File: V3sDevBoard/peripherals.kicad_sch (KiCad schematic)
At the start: 52 parts, among them J9 GPIO, SW1 BUT6, SW2 BUT1, SW3 BUT2, SW4 BUT3, SW5 BUT4, SW6 BUT5, U10 MPU-6050, U11 BME280, U8 ESP32-WROOM-32, U9 Ai-Thinker-Ra-02

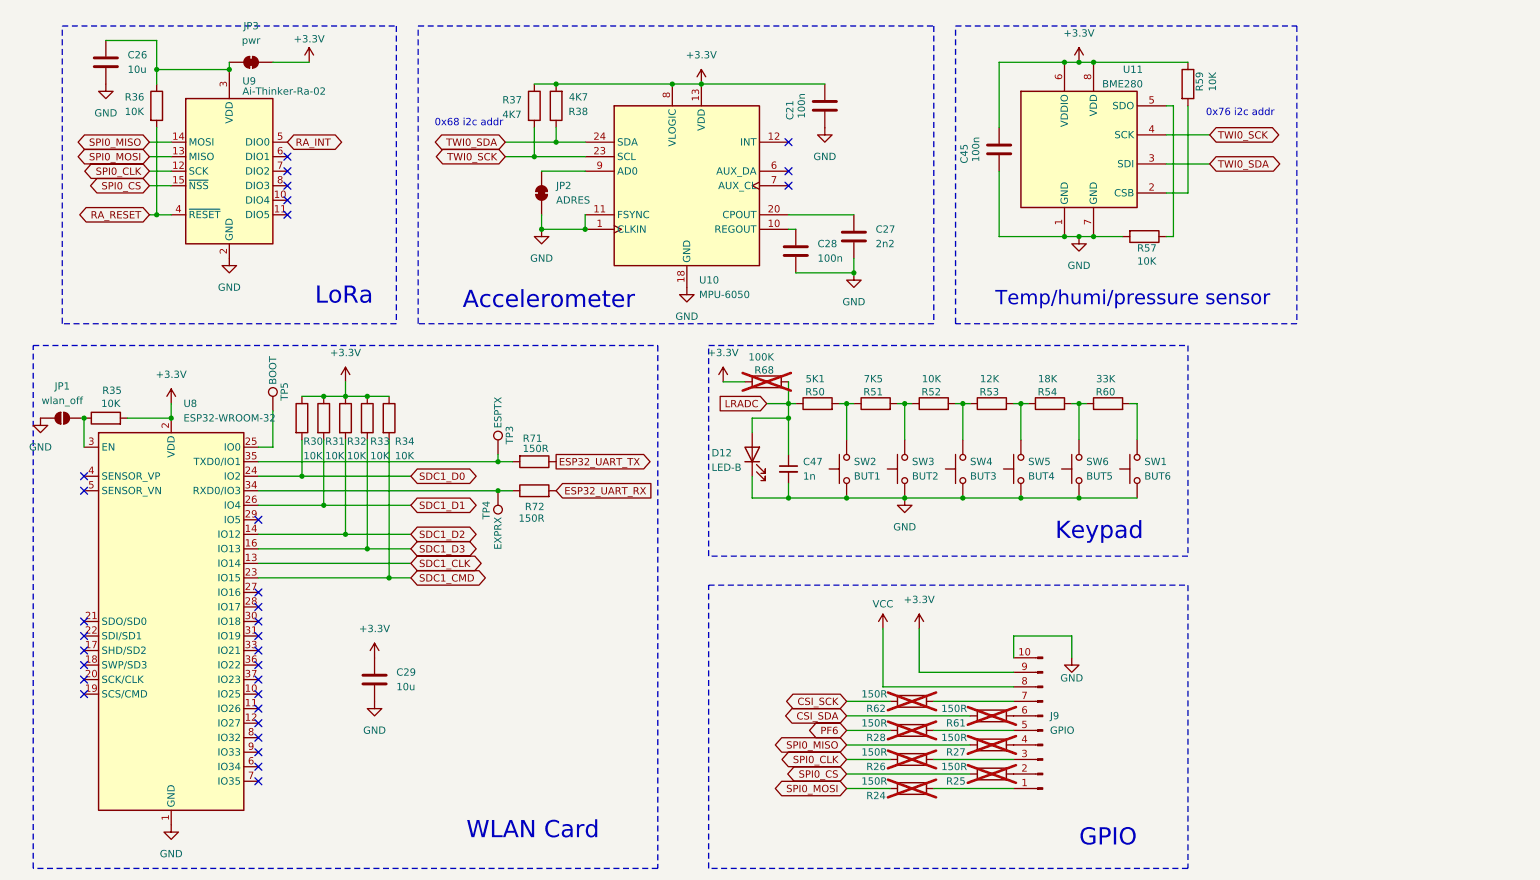
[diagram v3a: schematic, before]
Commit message: completing pcb desgin
Returning to project after month away. Switching to 4-layer desgin on 3313 stackup sig-gnd-pow-sig, changing size of some passive to 0603, connecting all components, adding silkscreen.
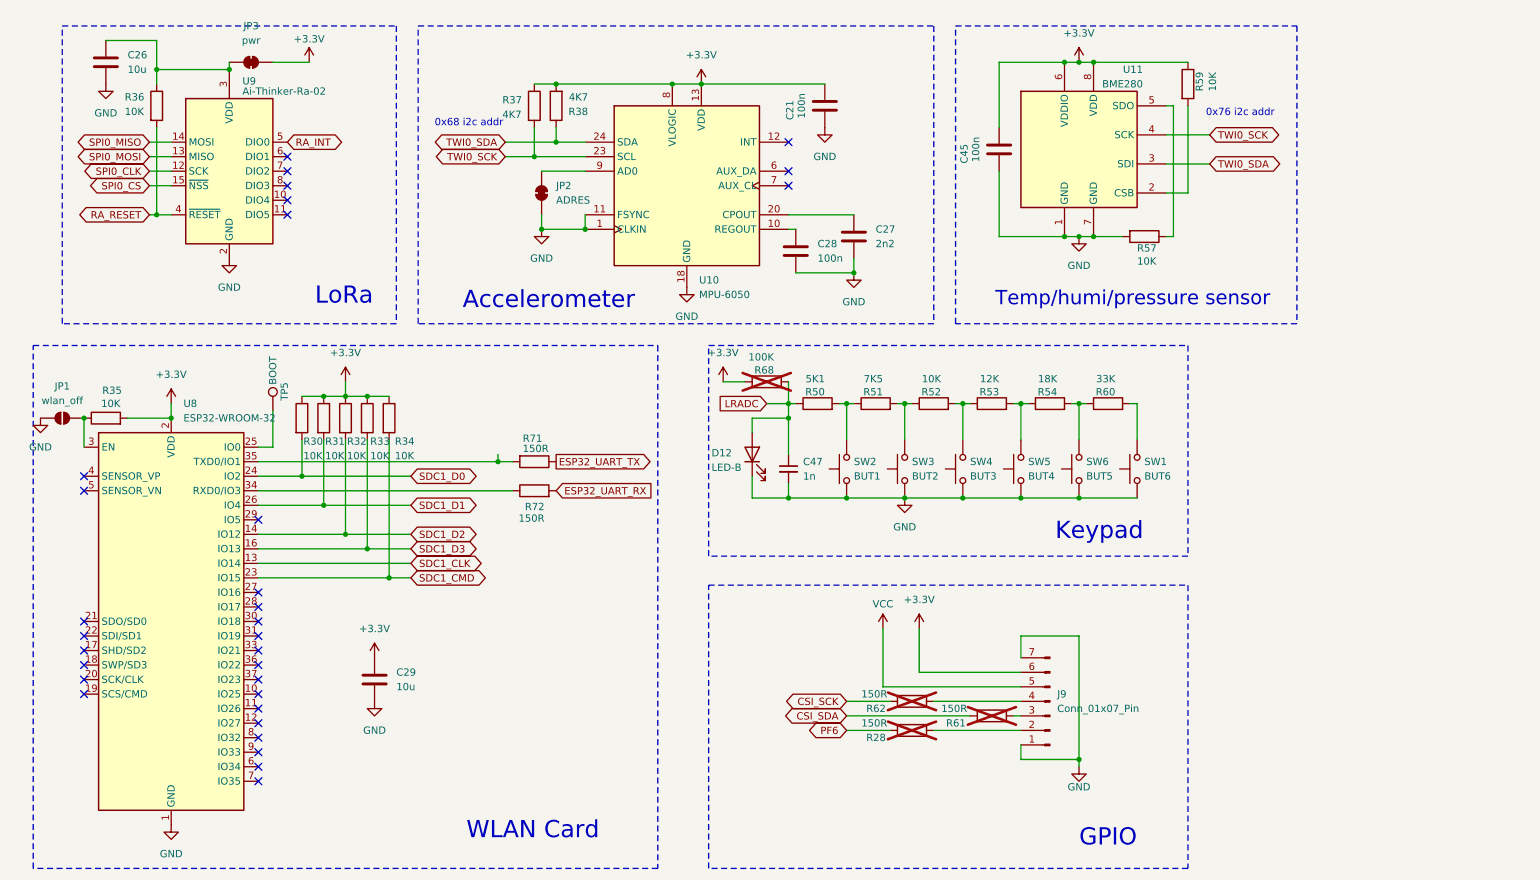
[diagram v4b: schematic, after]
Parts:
- removed J9: GPIO, Connector_PinHeader_2.54mm:PinHeader_1x10_P2.54mm_Vertical, symbol Connector:Conn_01x10_Pin
- removed R24, R25, R26, R27: 150R, Resistor_SMD:R_0805_2012Metric_Pad1.20x1.40mm_HandSolder, symbol Device:R
- removed TP3: ESPTX, TestPoint:TestPoint_Pad_D1.0mm, symbol Connector:TestPoint
- removed TP4: EXPRX, TestPoint:TestPoint_Pad_D1.0mm, symbol Connector:TestPoint
- added J9: Conn_01x07_Pin, Connector_PinHeader_2.54mm:PinHeader_1x07_P2.54mm_Vertical, symbol Connector:Conn_01x07_Pin
- C27, C28: footprint Capacitor_SMD:C_0805_2012Metric_Pad1.18x1.45mm_HandSolder -> Capacitor_SMD:C_0603_1608Metric_Pad1.08x0.95mm_HandSolder
- R28, R30, R31, R32, R33, R34, R35, R36, R37, R38, R50, R51, R52, R53, R54, R60, R61, R62, R68, R71, R72: footprint Resistor_SMD:R_0805_2012Metric_Pad1.20x1.40mm_HandSolder -> Resistor_SMD:R_0603_1608Metric_Pad0.98x0.95mm_HandSolder
- SW1, SW2, SW3, SW4, SW5, SW6: footprint Button_Switch_THT:SW_PUSH_6mm -> Button_Switch_SMD:Button_6x3mm
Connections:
- net +3.3V: now also J9.6 (Pin_6)
- net GND: now also J9.1 (Pin_1), J9.7 (Pin_7)
- net VCC: now also J9.5 (Pin_5)
- net at R28.2: now also J9.2 (Pin_2)
- net at R61.2: now also J9.3 (Pin_3)
- net at R62.2: now also J9.4 (Pin_4)

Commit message: last changes and sending to manufacturing
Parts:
- added R24: 1K, Resistor_SMD:R_0603_1608Metric_Pad0.98x0.95mm_HandSolder, symbol Device:R
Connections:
- net GND: now also R24.2
- net SDC1_D2: now also R24.1
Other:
- moved on the sheet: C29
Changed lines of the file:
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@@
 	)
 	(junction
+		(at 81.28 128.27)
+		(diameter 0)
+		(color 0 0 0 0)
+	)
+	(junction
 		(at 199.39 52.07)
 		(diameter 0)
@@
 		(color 0 0 0 0)
 	)
-	(junction
-		(at 95.25 91.44)
-		(diameter 0)
-		(color 0 0 0 0)
-	)
 	(no_connect
 		(at 22.86 124.46)
@@
 	(wire
 		(pts
-			(xy 186.69 121.92) (xy 186.69 125.73)
+			(xy 68.58 128.27) (xy 68.58 121.92)
 		)
 		(stroke
@@
 	(wire
 		(pts
-			(xy 162.56 120.65) (xy 162.56 130.81)
+			(xy 186.69 121.92) (xy 186.69 125.73)
 		)
 		(stroke
@@
 	(wire
 		(pts
-			(xy 76.2 111.76) (xy 53.34 111.76)
+			(xy 162.56 120.65) (xy 162.56 130.81)
 		)
 		(stroke
@@
 	(wire
 		(pts
-			(xy 34.29 43.18) (xy 38.1 43.18)
+			(xy 76.2 111.76) (xy 53.34 111.76)
 		)
 		(stroke
@@
 	(wire
 		(pts
-			(xy 95.25 91.44) (xy 97.79 91.44)
+			(xy 34.29 43.18) (xy 38.1 43.18)
 		)
 		(stroke
@@
 	(wire
 		(pts
-			(xy 157.48 81.28) (xy 156.21 81.28)
+			(xy 53.34 91.44) (xy 97.79 91.44)
 		)
 		(stroke
@@
 	(wire
 		(pts
-			(xy 176.53 97.79) (xy 186.69 97.79)
+			(xy 157.48 81.28) (xy 156.21 81.28)
 		)
 		(stroke
@@
 	(wire
 		(pts
-			(xy 95.25 90.17) (xy 95.25 91.44)
+			(xy 176.53 97.79) (xy 186.69 97.79)
 		)
 		(stroke
@@
 	(wire
 		(pts
+			(xy 68.58 114.3) (xy 68.58 104.14)
+		)
+		(stroke
+			(width 0)
+			(type default)
+		)
+	)
+	(wire
+		(pts
 			(xy 80.01 109.22) (xy 53.34 109.22)
 		)
@@
 	(wire
 		(pts
-			(xy 95.25 91.44) (xy 53.34 91.44)
-		)
-		(stroke
-			(width 0)
-			(type default)
-		)
-	)
-	(wire
-		(pts
 			(xy 215.9 21.59) (xy 199.39 21.59)
 		)
@@
 	(wire
 		(pts
-			(xy 55.88 21.59) (xy 62.23 21.59)
+			(xy 81.28 128.27) (xy 68.58 128.27)
 		)
 		(stroke
@@
 	(wire
 		(pts
-			(xy 80.01 104.14) (xy 68.58 104.14)
+			(xy 55.88 21.59) (xy 62.23 21.59)
 		)
 		(stroke
@@
 	(wire
 		(pts
+			(xy 68.58 104.14) (xy 80.01 104.14)
+		)
+		(stroke
+			(width 0)
+			(type default)
+		)
+	)
+	(wire
+		(pts
 			(xy 156.21 97.79) (xy 166.37 97.79)
 		)
@@
 	(symbol
 		(lib_id "power:+3.3V")
-		(at 73.66 125.73 0)
+		(at 81.28 120.65 0)
 		(unit 1)
 		(exclude_from_sim no)
@@
 		(fields_autoplaced yes)
 		(property "Reference" "#PWR071"
-			(at 73.66 129.54 0)
+			(at 81.28 124.46 0)
 			(effects
 				(font
@@
 		)
 		(property "Value" "+3.3V"
-			(at 73.66 120.65 0)
+			(at 81.28 115.57 0)
 			(effects
 				(font
@@
 		)
 		(property "Footprint" ""
-			(at 73.66 125.73 0)
+			(at 81.28 120.65 0)
 			(effects
 				(font
@@
 		)
 		(property "Datasheet" ""
-			(at 73.66 125.73 0)
+			(at 81.28 120.65 0)
 			(effects
 				(font
@@
 		)
 		(property "Description" "Power symbol creates a global label with name \"+3.3V\""
-			(at 73.66 125.73 0)
+			(at 81.28 120.65 0)
 			(effects
 				(font
@@
 	(symbol
 		(lib_id "Device:C")
-		(at 73.66 129.54 0)
+		(at 81.28 124.46 0)
 		(unit 1)
 		(exclude_from_sim no)
@@
 		(fields_autoplaced yes)
 		(property "Reference" "C29"
-			(at 77.47 128.2699 0)
+			(at 85.09 123.1899 0)
 			(effects
 				(font
@@
 		)
 		(property "Value" "10u"
-			(at 77.47 130.8099 0)
+			(at 85.09 125.7299 0)
 			(effects
 				(font
@@
 		)
 		(property "Footprint" "Capacitor_SMD:C_1206_3216Metric"
-			(at 74.6252 133.35 0)
+			(at 82.2452 128.27 0)
 			(effects
 				(font
@@
 		)
 		(property "Datasheet" "~"
-			(at 73.66 129.54 0)
+			(at 81.28 124.46 0)
 			(effects
 				(font
@@
 		)
 		(property "Description" "Unpolarized capacitor"
-			(at 73.66 129.54 0)
+			(at 81.28 124.46 0)
 			(effects
 				(font
@@
 	(symbol
 		(lib_id "power:GND")
-		(at 73.66 133.35 0)
+		(at 81.28 128.27 0)
 		(unit 1)
 		(exclude_from_sim no)
@@
 		(fields_autoplaced yes)
 		(property "Reference" "#PWR072"
-			(at 73.66 139.7 0)
+			(at 81.28 134.62 0)
 			(effects
 				(font
@@
 		)
 		(property "Value" "GND"
-			(at 73.66 138.43 0)
+			(at 81.28 133.35 0)
 			(effects
 				(font
@@
 		)
 		(property "Footprint" ""
-			(at 73.66 133.35 0)
+			(at 81.28 128.27 0)
 			(effects
 				(font
@@
 		)
 		(property "Datasheet" ""
-			(at 73.66 133.35 0)
+			(at 81.28 128.27 0)
 			(effects
 				(font
@@
 		)
 		(property "Description" "Power symbol creates a global label with name \"GND\" , ground"
-			(at 73.66 133.35 0)
+			(at 81.28 128.27 0)
 			(effects
 				(font
@@
 					(unit 1)
 				)
+			)
+		)
+	)
+	(symbol
+		(lib_id "Device:R")
+		(at 68.58 118.11 0)
+		(unit 1)
+		(exclude_from_sim no)
+		(in_bom yes)
+		(on_board yes)
+		(dnp yes)
+		(property "Reference" "R24"
+			(at 68.834 122.174 0)
+			(effects
+				(font
+					(size 1.27 1.27)
+				)
+				(justify left)
+			)
+		)
+		(property "Value" "1K"
+			(at 68.834 124.714 0)
+			(effects
+				(font
+					(size 1.27 1.27)
+				)
+				(justify left)
+			)
+		)
+		(property "Footprint" "Resistor_SMD:R_0603_1608Metric_Pad0.98x0.95mm_HandSolder"
+			(at 66.802 118.11 90)
+			(effects
+				(font
+					(size 1.27 1.27)
+				)
+				(hide yes)
+			)
+		)
+		(property "Datasheet" "~"
+			(at 68.58 118.11 0)
+			(effects
+				(font
+					(size 1.27 1.27)
+				)
+				(hide yes)
+			)
+		)
+		(property "Description" "Resistor"
+			(at 68.58 118.11 0)
+			(effects
+				(font
+					(size 1.27 1.27)
+				)
+				(hide yes)
+			)
+		)
+		(pin "2"
+		)
+		(pin "1"
+		)
+		(instances
+			(project "V3sDevBoard"
+				(path "/e07febb4-5889-4da3-b279-3be53a5a6756/6b4bd028-5763-47d7-84d2-48e153976a13"
+					(reference "R24")
+					(unit 1)
+				)
